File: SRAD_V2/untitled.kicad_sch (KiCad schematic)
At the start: 12 parts, among them U13 KX134-1211, U14 MAX-M10S, U15 MS5607-02BA, U16 MMC5983MA, U17 ASM330LHH, U18 MCP9808_DFN, U19 AS5F31G04SND-08LIN

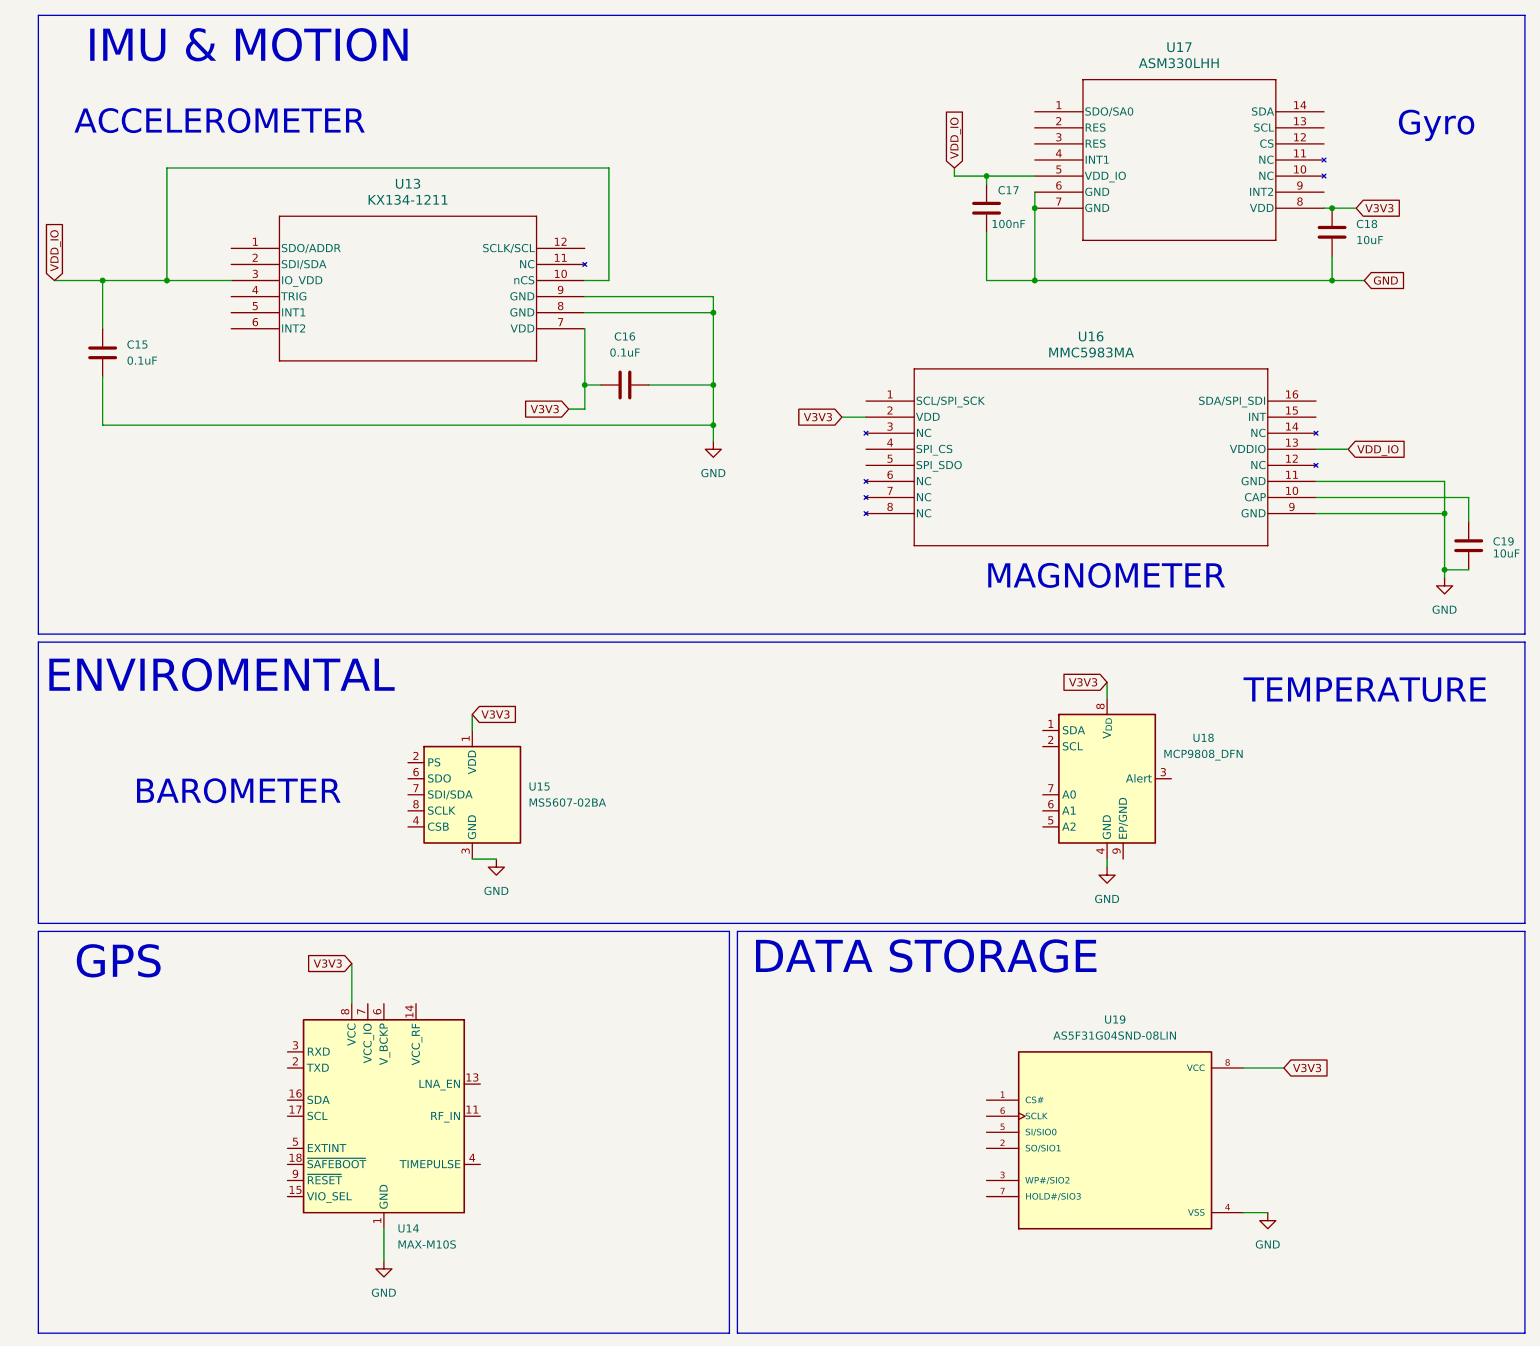
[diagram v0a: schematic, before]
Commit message: created some basic building blocks as hierarchical sheets
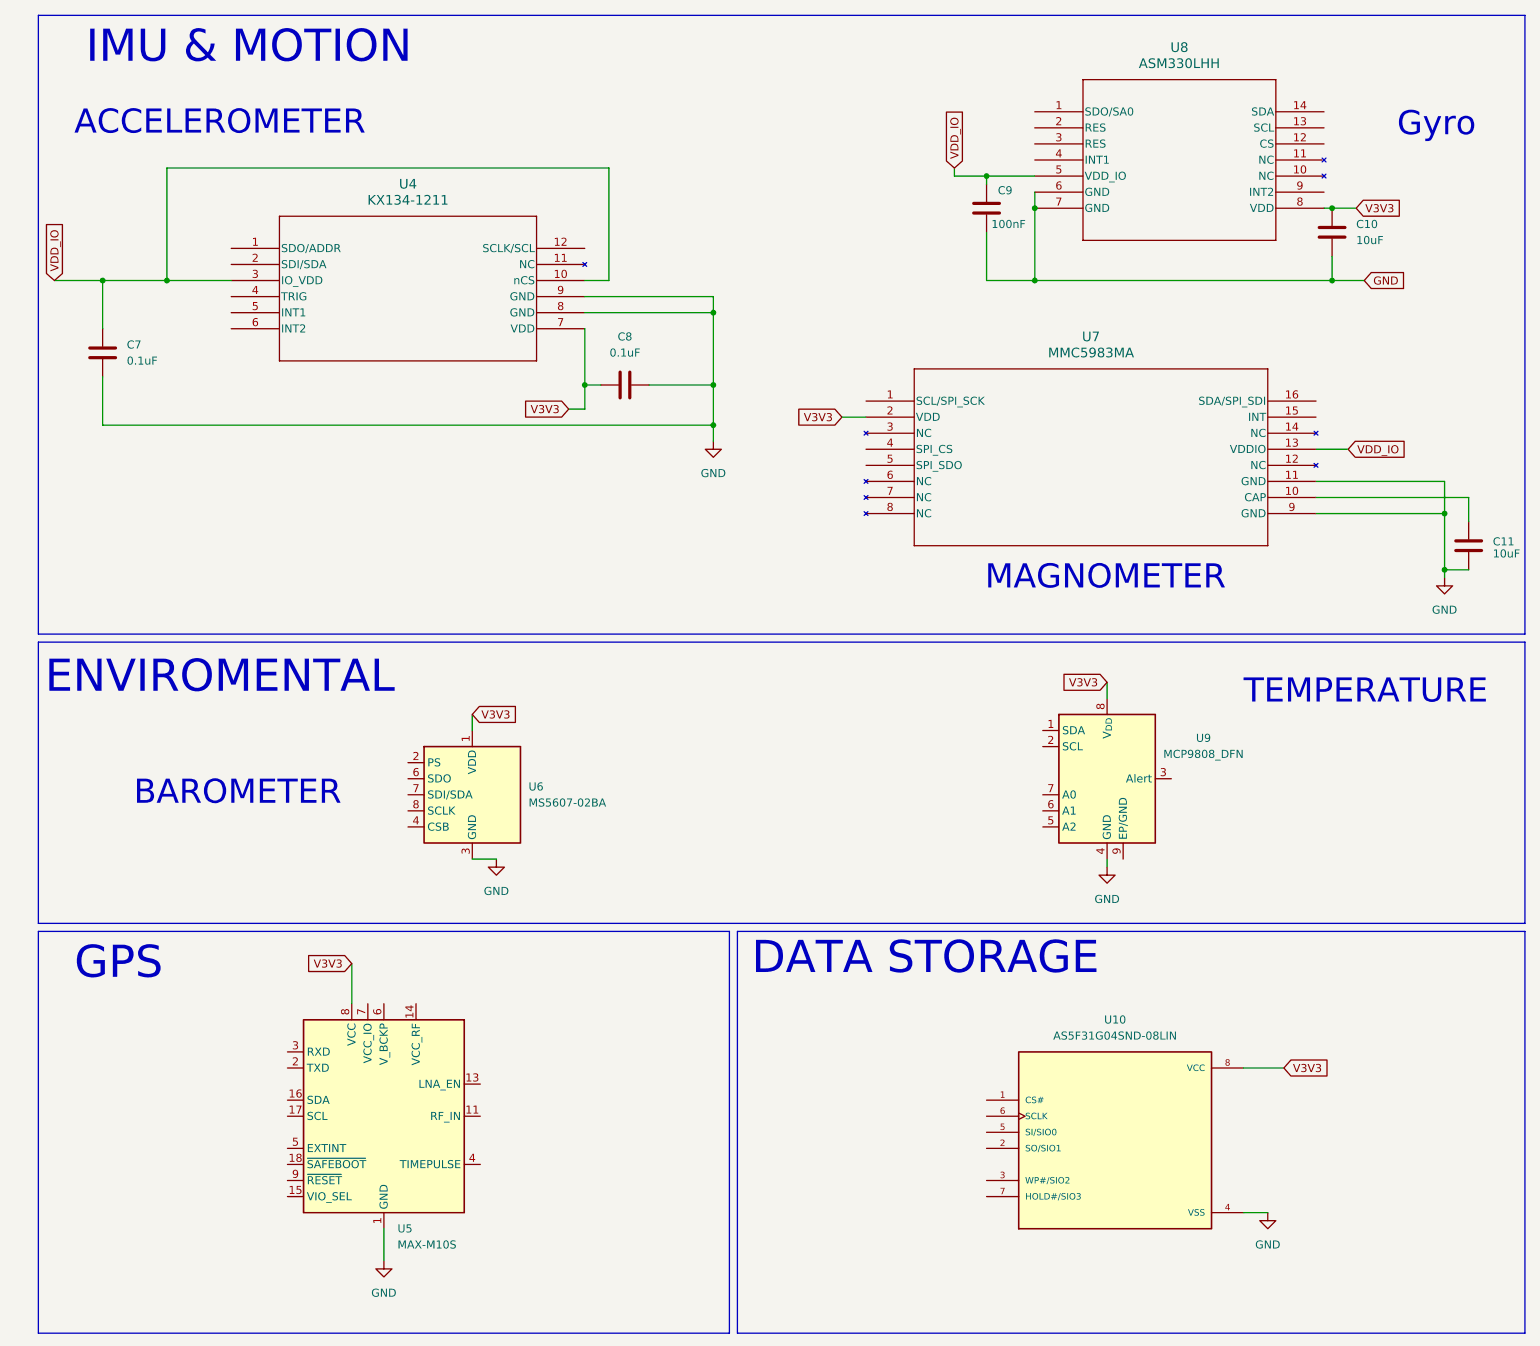
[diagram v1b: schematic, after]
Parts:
- renumbered C18 to C10, C19 to C11, C15 to C7, C16 to C8, C17 to C9, U19 to U10, U13 to U4, U14 to U5, U15 to U6, U16 to U7, U17 to U8, U18 to U9
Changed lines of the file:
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@@
 		(on_board yes)
 		(dnp no)
-		(property "Reference" "U16"
+		(property "Reference" "U7"
 			(at 246.38 85.09 0)
 			(effects
@@
 			(project "SRAD_V2"
 				(path "/016ea6e5-09c6-43d4-b6cc-3404e2d65458/ac92d8dd-ef30-4ac9-90eb-deb18ea006aa"
-					(reference "U16")
+					(reference "U7")
 					(unit 1)
 				)
@@
 		(dnp no)
 		(fields_autoplaced yes)
-		(property "Reference" "C18"
+		(property "Reference" "C10"
 			(at 288.29 67.3099 0)
 			(effects
@@
 			(project "SRAD_V2"
 				(path "/016ea6e5-09c6-43d4-b6cc-3404e2d65458/ac92d8dd-ef30-4ac9-90eb-deb18ea006aa"
-					(reference "C18")
+					(reference "C10")
 					(unit 1)
 				)
@@
 		(dnp no)
 		(fields_autoplaced yes)
-		(property "Reference" "#PWR028"
+		(property "Reference" "#PWR019"
 			(at 274.32 229.87 0)
 			(effects
@@
 			(project "SRAD_V2"
 				(path "/016ea6e5-09c6-43d4-b6cc-3404e2d65458/ac92d8dd-ef30-4ac9-90eb-deb18ea006aa"
-					(reference "#PWR028")
+					(reference "#PWR019")
 					(unit 1)
 				)
@@
 		(dnp no)
 		(fields_autoplaced yes)
-		(property "Reference" "U13"
+		(property "Reference" "U4"
 			(at 138.43 60.96 0)
 			(effects
@@
 			(project "SRAD_V2"
 				(path "/016ea6e5-09c6-43d4-b6cc-3404e2d65458/ac92d8dd-ef30-4ac9-90eb-deb18ea006aa"
-					(reference "U13")
+					(reference "U4")
 					(unit 1)
 				)
@@
 		(on_board yes)
 		(dnp no)
-		(property "Reference" "C17"
+		(property "Reference" "C9"
 			(at 231.648 61.976 0)
 			(effects
@@
 			(project "SRAD_V2"
 				(path "/016ea6e5-09c6-43d4-b6cc-3404e2d65458/ac92d8dd-ef30-4ac9-90eb-deb18ea006aa"
-					(reference "C17")
+					(reference "C9")
 					(unit 1)
 				)
@@
 		(dnp no)
 		(fields_autoplaced yes)
-		(property "Reference" "U15"
+		(property "Reference" "U6"
 			(at 157.48 156.2099 0)
 			(effects
@@
 			(project "SRAD_V2"
 				(path "/016ea6e5-09c6-43d4-b6cc-3404e2d65458/ac92d8dd-ef30-4ac9-90eb-deb18ea006aa"
-					(reference "U15")
+					(reference "U6")
 					(unit 1)
 				)
@@
 		(dnp no)
 		(fields_autoplaced yes)
-		(property "Reference" "#PWR025"
+		(property "Reference" "#PWR016"
 			(at 152.4 173.99 0)
 			(effects
@@
 			(project "SRAD_V2"
 				(path "/016ea6e5-09c6-43d4-b6cc-3404e2d65458/ac92d8dd-ef30-4ac9-90eb-deb18ea006aa"
-					(reference "#PWR025")
+					(reference "#PWR016")
 					(unit 1)
 				)
@@
 		(dnp no)
 		(fields_autoplaced yes)
-		(property "Reference" "#PWR027"
+		(property "Reference" "#PWR018"
 			(at 248.92 175.26 0)
 			(effects
@@
 			(project "SRAD_V2"
 				(path "/016ea6e5-09c6-43d4-b6cc-3404e2d65458/ac92d8dd-ef30-4ac9-90eb-deb18ea006aa"
-					(reference "#PWR027")
+					(reference "#PWR018")
 					(unit 1)
 				)
@@
 		(dnp no)
 		(fields_autoplaced yes)
-		(property "Reference" "C15"
+		(property "Reference" "C7"
 			(at 93.98 86.3599 0)
 			(effects
@@
 			(project "SRAD_V2"
 				(path "/016ea6e5-09c6-43d4-b6cc-3404e2d65458/ac92d8dd-ef30-4ac9-90eb-deb18ea006aa"
-					(reference "C15")
+					(reference "C7")
 					(unit 1)
 				)
@@
 		(dnp no)
 		(fields_autoplaced yes)
-		(property "Reference" "U14"
+		(property "Reference" "U5"
 			(at 136.7633 226.06 0)
 			(effects
@@
 			(project "SRAD_V2"
 				(path "/016ea6e5-09c6-43d4-b6cc-3404e2d65458/ac92d8dd-ef30-4ac9-90eb-deb18ea006aa"
-					(reference "U14")
+					(reference "U5")
 					(unit 1)
 				)
@@
 		(dnp no)
 		(fields_autoplaced yes)
-		(property "Reference" "U18"
+		(property "Reference" "U9"
 			(at 264.16 148.5198 0)
 			(effects
@@
 			(project "SRAD_V2"
 				(path "/016ea6e5-09c6-43d4-b6cc-3404e2d65458/ac92d8dd-ef30-4ac9-90eb-deb18ea006aa"
-					(reference "U18")
+					(reference "U9")
 					(unit 1)
 				)
@@
 		(dnp no)
 		(fields_autoplaced yes)
-		(property "Reference" "#PWR026"
+		(property "Reference" "#PWR017"
 			(at 186.69 107.95 0)
 			(effects
@@
 			(project "SRAD_V2"
 				(path "/016ea6e5-09c6-43d4-b6cc-3404e2d65458/ac92d8dd-ef30-4ac9-90eb-deb18ea006aa"
-					(reference "#PWR026")
+					(reference "#PWR017")
 					(unit 1)
 				)
@@
 		(dnp no)
 		(fields_autoplaced yes)
-		(property "Reference" "U19"
+		(property "Reference" "U10"
 			(at 250.19 193.04 0)
 			(effects
@@
 			(project "SRAD_V2"
 				(path "/016ea6e5-09c6-43d4-b6cc-3404e2d65458/ac92d8dd-ef30-4ac9-90eb-deb18ea006aa"
-					(reference "U19")
+					(reference "U10")
 					(unit 1)
 				)
@@
 		(dnp no)
 		(fields_autoplaced yes)
-		(property "Reference" "C19"
+		(property "Reference" "C11"
 			(at 309.88 117.4749 0)
 			(effects
@@
 			(project "SRAD_V2"
 				(path "/016ea6e5-09c6-43d4-b6cc-3404e2d65458/ac92d8dd-ef30-4ac9-90eb-deb18ea006aa"
-					(reference "C19")
+					(reference "C11")
 					(unit 1)
 				)
@@
 		(dnp no)
 		(fields_autoplaced yes)
-		(property "Reference" "U17"
+		(property "Reference" "U8"
 			(at 260.35 39.37 0)
 			(effects
@@
 			(project "SRAD_V2"
 				(path "/016ea6e5-09c6-43d4-b6cc-3404e2d65458/ac92d8dd-ef30-4ac9-90eb-deb18ea006aa"
-					(reference "U17")
+					(reference "U8")
 					(unit 1)
 				)
@@
 		(dnp no)
 		(fields_autoplaced yes)
-		(property "Reference" "C16"
+		(property "Reference" "C8"
 			(at 172.72 85.09 90)
 			(effects
@@
 			(project "SRAD_V2"
 				(path "/016ea6e5-09c6-43d4-b6cc-3404e2d65458/ac92d8dd-ef30-4ac9-90eb-deb18ea006aa"
-					(reference "C16")
+					(reference "C8")
 					(unit 1)
 				)
@@
 		(dnp no)
 		(fields_autoplaced yes)
-		(property "Reference" "#PWR024"
+		(property "Reference" "#PWR015"
 			(at 134.62 237.49 0)
 			(effects
@@
 			(project "SRAD_V2"
 				(path "/016ea6e5-09c6-43d4-b6cc-3404e2d65458/ac92d8dd-ef30-4ac9-90eb-deb18ea006aa"
-					(reference "#PWR024")
+					(reference "#PWR015")
 					(unit 1)
 				)
@@
 		(dnp no)
 		(fields_autoplaced yes)
-		(property "Reference" "#PWR029"
+		(property "Reference" "#PWR020"
 			(at 302.26 129.54 0)
 			(effects
@@
 			(project "SRAD_V2"
 				(path "/016ea6e5-09c6-43d4-b6cc-3404e2d65458/ac92d8dd-ef30-4ac9-90eb-deb18ea006aa"
-					(reference "#PWR029")
-					(unit 1)
-				)
+					(reference "#PWR020")
+					(unit 1)
+				)

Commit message: linked 3-d models
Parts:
- U10: footprint AS5F31G04SND-08LIN:SON127P600X800X80-8N -> NAND_Flash:SON127P600X800X80-8N
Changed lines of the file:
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@@
 			)
 		)
-		(property "Footprint" "AS5F31G04SND-08LIN:SON127P600X800X80-8N"
+		(property "Footprint" "NAND_Flash:SON127P600X800X80-8N"
 			(at 250.19 213.36 0)
 			(effects

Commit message: more changes
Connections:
- net V3V3 renamed +3V3
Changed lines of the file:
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@@
 		)
 	)
-	(global_label "V3V3"
+	(global_label "+3V3"
 		(shape input)
 		(at 129.54 184.15 180)
@@
 		)
 	)
-	(global_label "V3V3"
+	(global_label "+3V3"
 		(shape input)
 		(at 148.59 144.78 0)
@@
 		)
 	)
-	(global_label "V3V3"
+	(global_label "+3V3"
 		(shape input)
 		(at 288.29 64.77 0)
@@
 		)
 	)
-	(global_label "V3V3"
+	(global_label "+3V3"
 		(shape input)
 		(at 163.83 96.52 180)
@@
 		)
 	)
-	(global_label "V3V3"
+	(global_label "+3V3"
 		(shape input)
 		(at 207.01 97.79 180)
@@
 		)
 	)
-	(global_label "V3V3"
+	(global_label "+3V3"
 		(shape input)
 		(at 276.86 200.66 0)
@@
 		)
 	)
-	(global_label "V3V3"
+	(global_label "+3V3"
 		(shape input)
 		(at 248.92 139.7 180)
